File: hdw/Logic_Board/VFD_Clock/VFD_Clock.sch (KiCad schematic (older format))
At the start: 0 parts

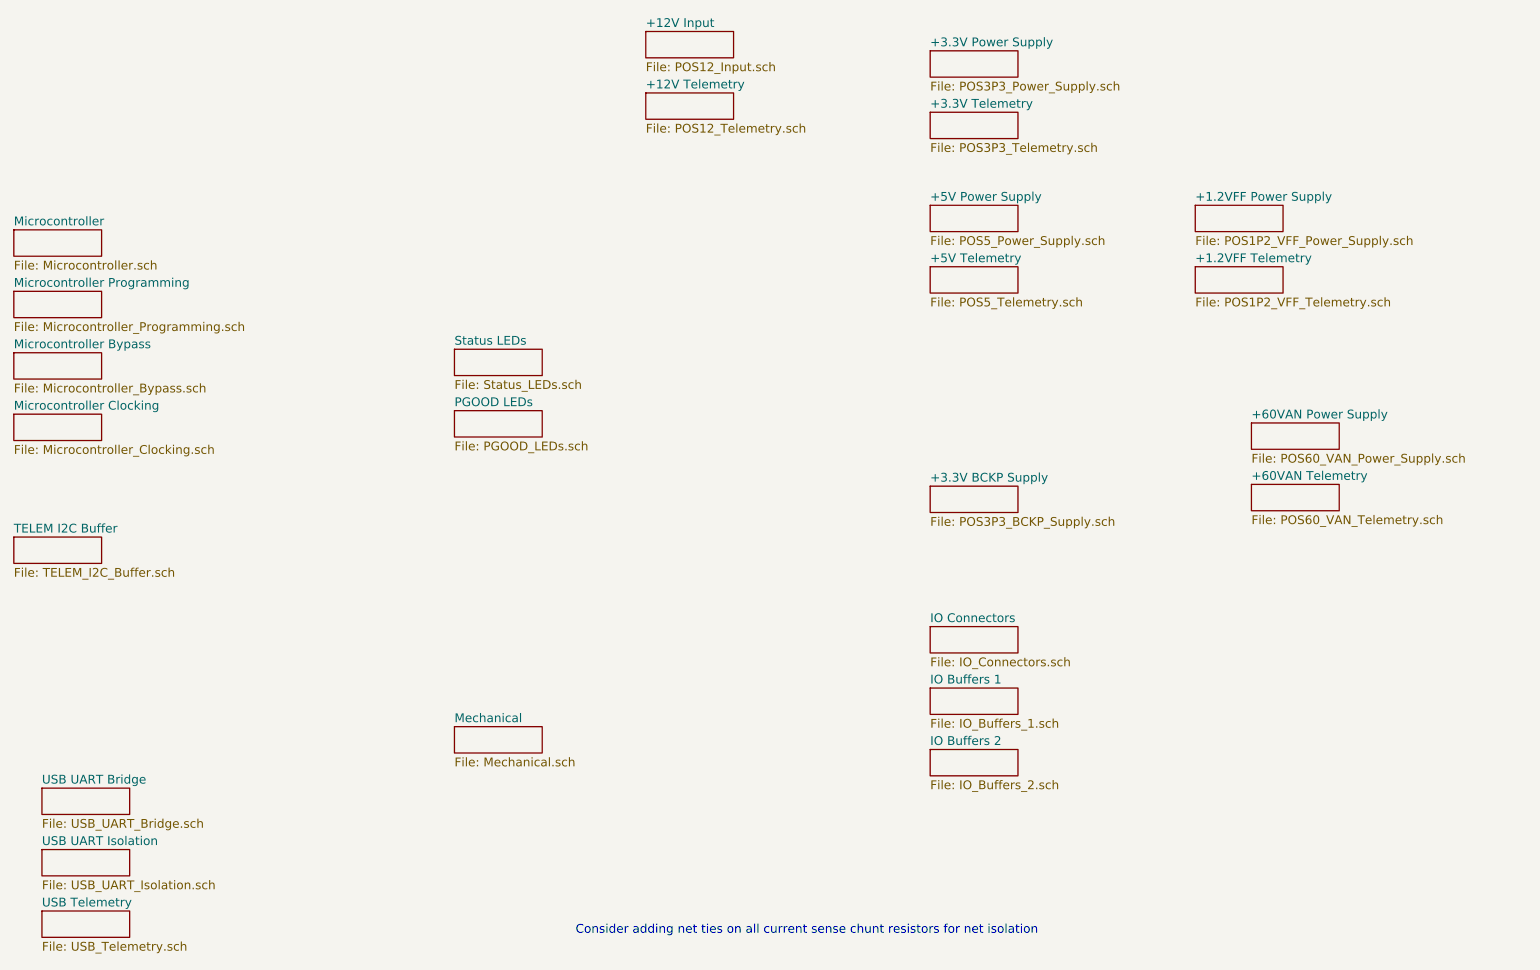
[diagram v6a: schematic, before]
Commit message: Lots of schematic additions
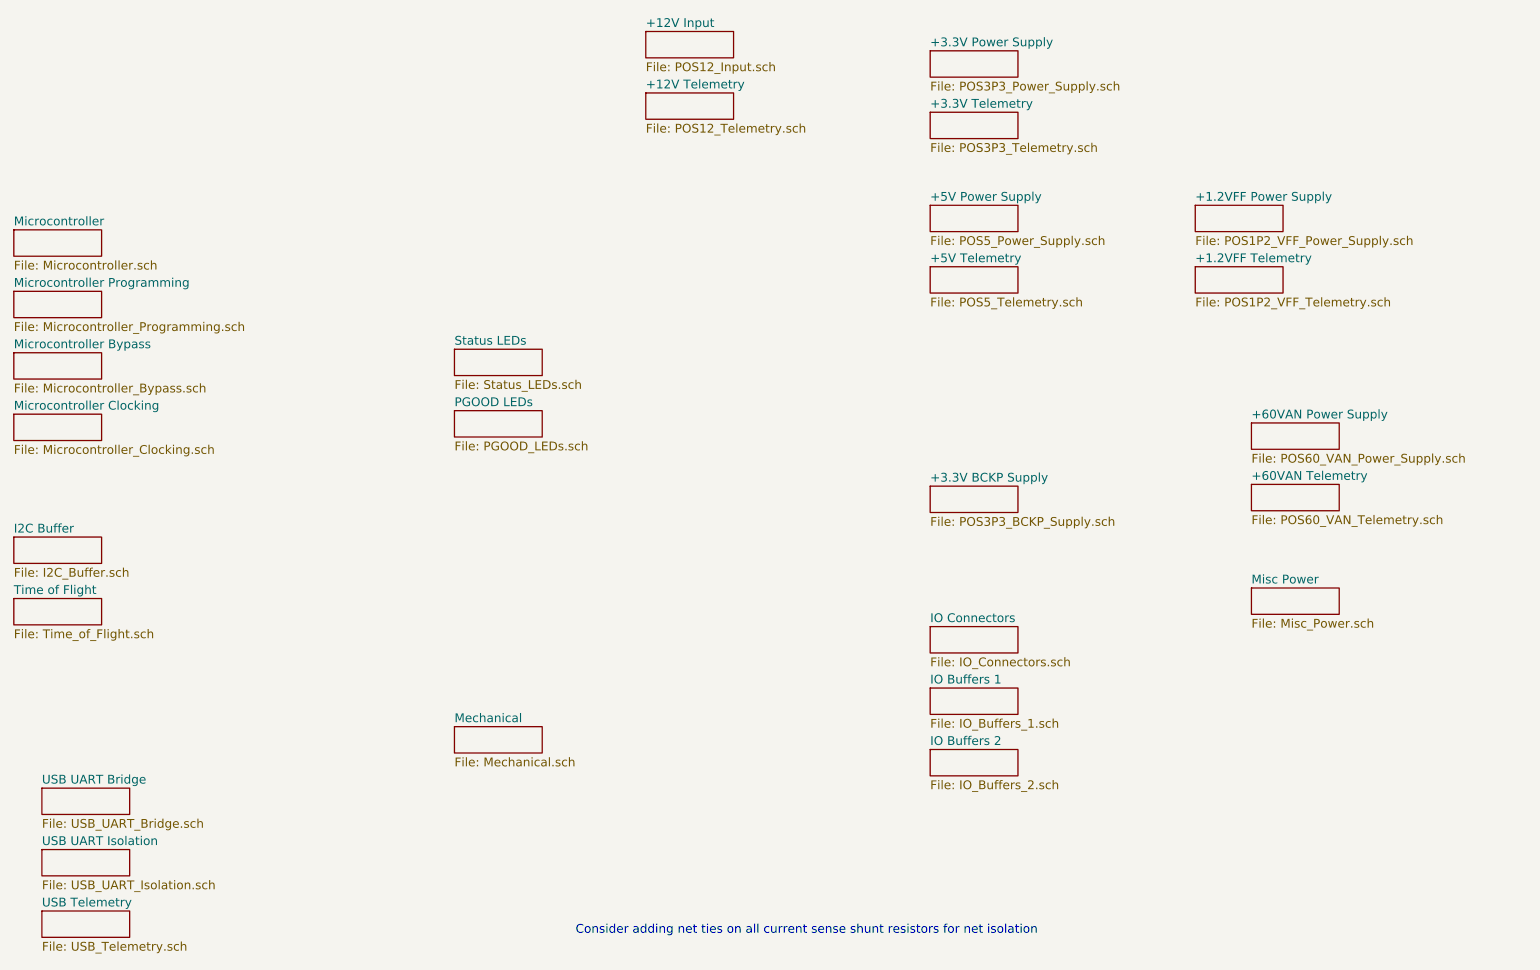
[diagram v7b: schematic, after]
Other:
- note added: "Consider adding net ties on all current sense shunt resistors for net isolation"
- note removed: "Consider adding net ties on all current sense chunt resistors for net isolation"
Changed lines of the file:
@@
 $Descr A 11000 8500
 encoding utf-8
-Sheet 1 26
+Sheet 1 28
 Title "VFD Clock"
 Date "2019-04-11"
@@
 S 1180 4000 500  150
 U 5E0CF7BC
-F0 "TELEM I2C Buffer" 50
-F1 "TELEM_I2C_Buffer.sch" 50
+F0 "I2C Buffer" 50
+F1 "I2C_Buffer.sch" 50
 $EndSheet
 $Sheet
@@
 $EndSheet
 Text Notes 4380 6270 0    50   ~ 0
-Consider adding net ties on all current sense chunt resistors for net isolation
+Consider adding net ties on all current sense shunt resistors for net isolation
+$Sheet
+S 1180 4350 500  150
+U 5E07B870
+F0 "Time of Flight" 50
+F1 "Time_of_Flight.sch" 50
+$EndSheet
+$Sheet
+S 8230 4290 500  150
+U 5E1352F5
+F0 "Misc Power" 50
+F1 "Misc_Power.sch" 50
+$EndSheet
 $EndSCHEMATC

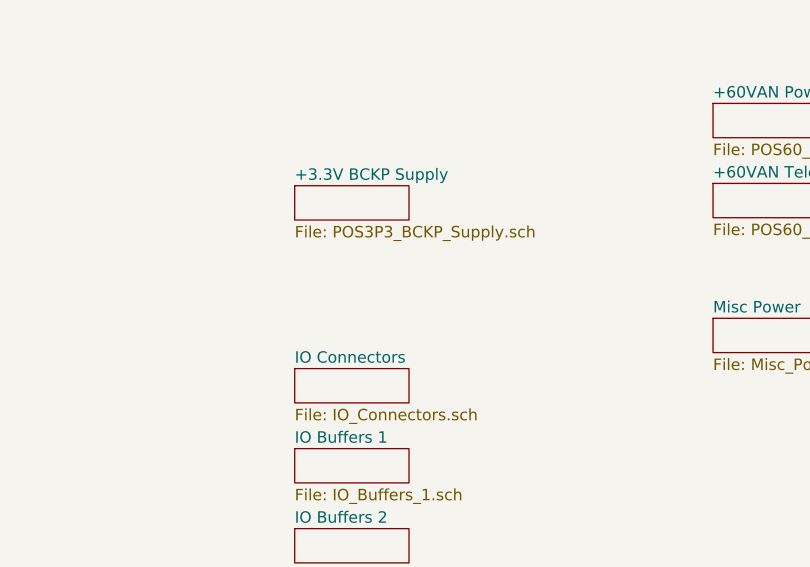
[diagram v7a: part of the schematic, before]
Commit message: Added backup RTC, IO connector, other stuff
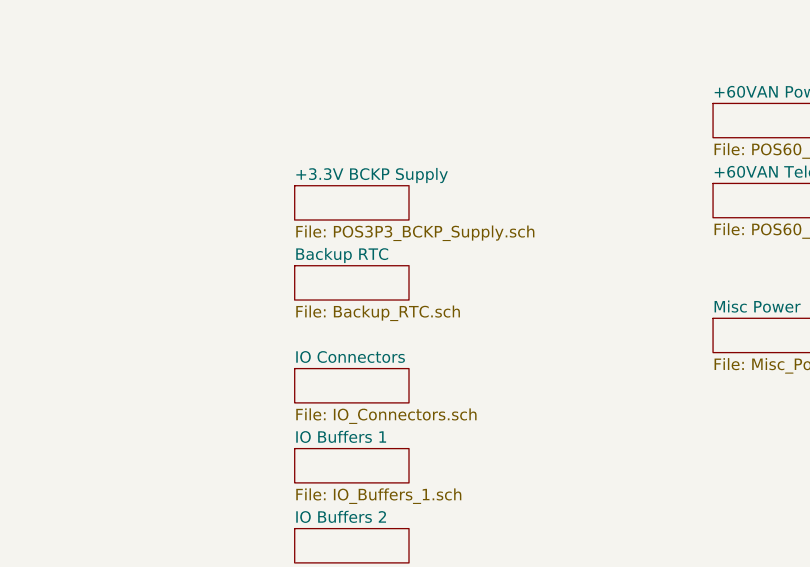
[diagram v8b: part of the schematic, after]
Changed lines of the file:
@@
 $Descr A 11000 8500
 encoding utf-8
-Sheet 1 28
+Sheet 1 29
 Title "VFD Clock"
 Date "2019-04-11"
@@
 F1 "Misc_Power.sch" 50
 $EndSheet
+$Sheet
+S 6400 4060 500  150
+U 5E213465
+F0 "Backup RTC" 50
+F1 "Backup_RTC.sch" 50
+$EndSheet
 $EndSCHEMATC
